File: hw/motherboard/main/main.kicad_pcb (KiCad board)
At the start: 4 copper layers, 100 x 100 mm, 104 parts, among them J1 SWD holes, J2 Conn_ARM_JTAG_SWD_10, J3 690-005-299-043, J4 STACK_GND, Q1 BSS138, SW1 SW_Push, U1 STM32F303RETx, U2 FT232RL-REEL, Y1 HSE

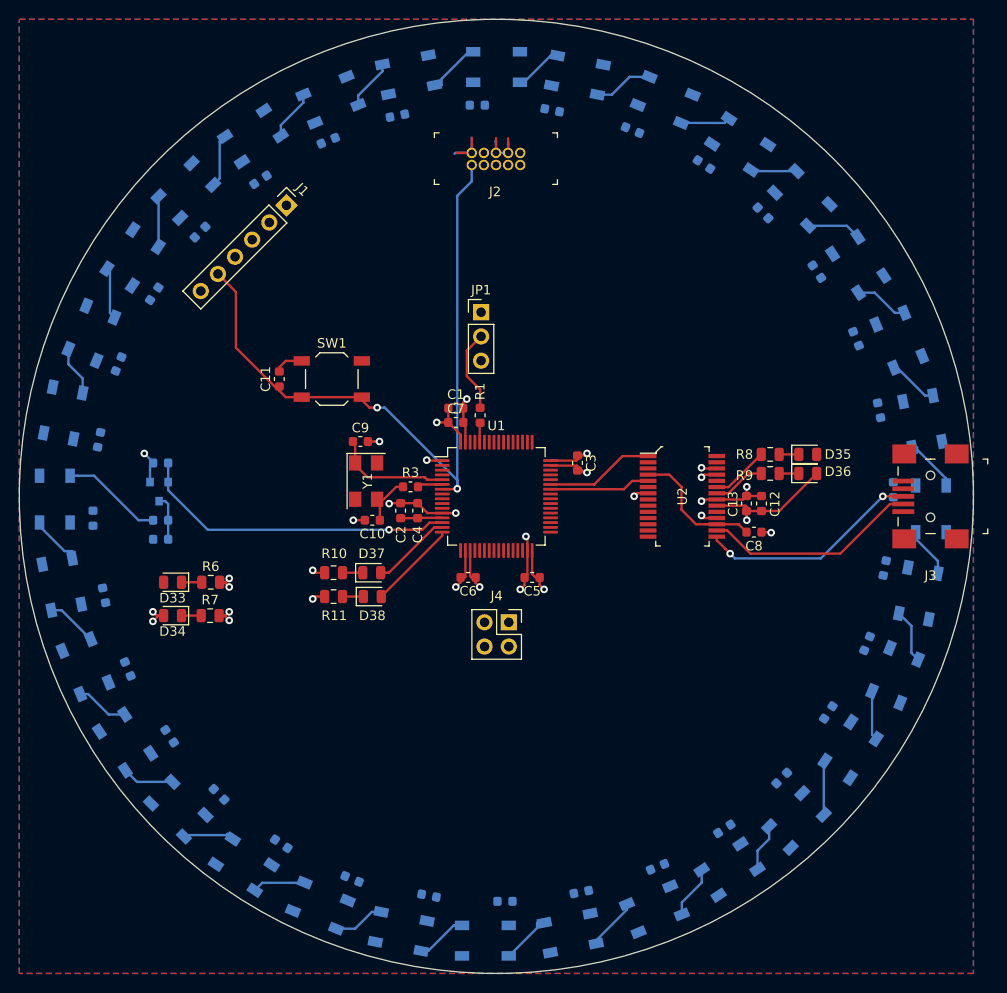
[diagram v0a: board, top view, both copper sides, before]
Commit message: WIP Add electromagnet and sensor schematic connections to MCU pins
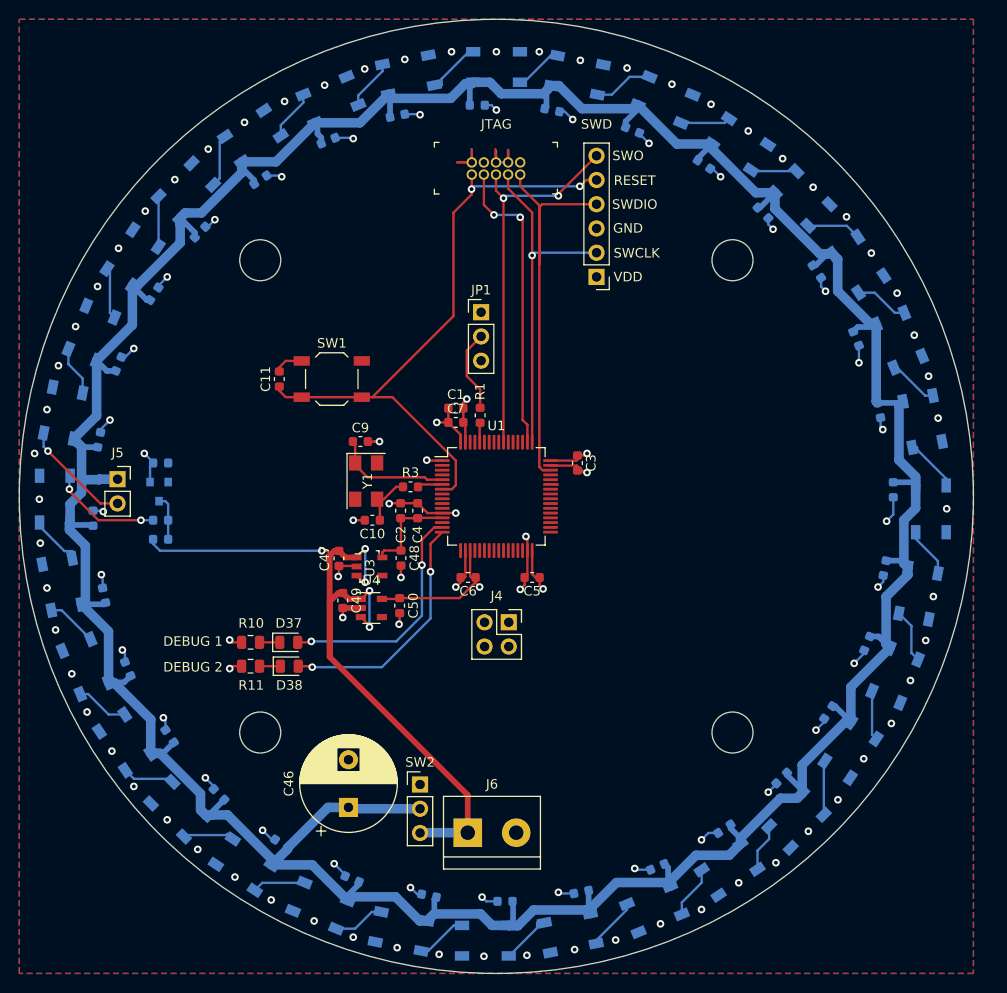
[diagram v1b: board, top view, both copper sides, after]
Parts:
- removed C12: 4.7u, Capacitor_SMD:C_0603_1608Metric
- removed C13, C8: 100n, Capacitor_SMD:C_0603_1608Metric
- removed D33: LED_5V, LED_SMD:LED_0805_2012Metric
- removed D34: LED_3V3, LED_SMD:LED_0805_2012Metric
- removed D35: LED_TX, LED_SMD:LED_0805_2012Metric
- removed D36: LED_RX, LED_SMD:LED_0805_2012Metric
- removed J3: 690-005-299-043, digikey-footprints:USB_Mini_B_Female_690-005-299-043
- removed R6, R7: TBD, Resistor_SMD:R_0805_2012Metric
- removed R8, R9: 1k, Resistor_SMD:R_0805_2012Metric
- removed U2: FT232RL-REEL, digikey-footprints:SSOP-28_W5.30mm
- added C46: 1000u, Capacitor_THT:CP_Radial_D10.0mm_P5.00mm, F.Cu at (134.5, 132.6)
- added C47: 1u, Capacitor_SMD:C_0603_1608Metric, F.Cu at (133.5, 106.5)
- added C48: 1u, Capacitor_SMD:C_0603_1608Metric, F.Cu at (140.0, 106.5)
- added C49: 1u, Capacitor_SMD:C_0603_1608Metric, F.Cu at (133.9, 110.9)
- added C50: 1u, Capacitor_SMD:C_0603_1608Metric, F.Cu at (139.9, 111.5)
- added H1: MountingHole, MountingHole:MountingHole_4.3mm_M4, F.Cu at (174.7, 124.7)
- added H2: MountingHole, MountingHole:MountingHole_4.3mm_M4, F.Cu at (125.3, 124.7)
- added H3: MountingHole, MountingHole:MountingHole_4.3mm_M4, F.Cu at (125.3, 75.3)
- added H4: MountingHole, MountingHole:MountingHole_4.3mm_M4, F.Cu at (174.7, 75.3)
- added J5: RGB stack, Connector_PinSocket_2.54mm:PinSocket_1x02_P2.54mm_Vertical, F.Cu at (110.3, 98.2)
- added J6: 5V power in, TerminalBlock:TerminalBlock_bornier-2_P5.08mm, F.Cu at (147.0, 135.2)
- added SW2: SW_SPDT, Connector_PinHeader_2.54mm:PinHeader_1x03_P2.54mm_Vertical, F.Cu at (142.0, 130.2)
- added U3: LP5907MFX-3_3_NOPB, digikey-footprints:SOT-753, F.Cu at (136.7, 107.3)
- added U4: TLV75533PDBV, Package_TO_SOT_SMD:SOT-23-5, F.Cu at (136.9, 111.7)
- moved J1 33.4 mm to (160.5, 77.0), turned to 180 degrees
- moved R10 11.4 mm to (124.2, 115.3)
- moved R11 11.4 mm to (124.2, 117.8)
- moved D37 11.4 mm to (128.2, 115.3)
- moved D38 11.4 mm to (128.3, 117.8)
- moved J2 1.00 mm to (152.5, 65.0)
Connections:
- net +5V renamed /rgb/5V_RGB
- U1 pad 14: /rgb/DIN -> Net-(U1-Pad14)
- U1 pad 4: Net-(U1-Pad4) -> /rgb/DIN
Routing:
- net /rgb/5V_RGB: track 13.6 -> 405.7 mm, vias 1 -> 0
- net +5V: track 0.00 -> 86.5 mm, vias 0 -> 5
- net /JTAG_TMS: track 0.00 -> 44.9 mm
- net /JTAG_TDO: track 0.00 -> 40.1 mm, vias 0 -> 2
- net GND: track 74.6 -> 112.7 mm, vias 22 -> 109
- net /JTAG_TCK: track 0.00 -> 36.0 mm, vias 0 -> 1
- net /rgb/DIN: track 33.6 -> 0.00 mm, vias 1 -> 0
- net /JTAG_TDI: track 0.00 -> 31.4 mm, vias 0 -> 2
- net /USB_DP: track 23.4 -> 0.00 mm, vias 2 -> 0
- net /USB_DM: track 22.7 -> 0.00 mm
- net /DEBUG_1: track 8.42 -> 24.8 mm, vias 0 -> 2
- net /DEBUG_2: track 9.40 -> 25.6 mm, vias 0 -> 2
- net Net-(C8-Pad1): track 14.2 -> 0.00 mm
- net Net-(D32-Pad2): track 0.00 -> 11.7 mm, vias 0 -> 1
- net /USART1_RX: track 11.5 -> 0.77 mm
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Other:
- net class power added: clearance 1, trace_width 0.25, via_dia 0.8, via_drill 0.4
- board text added: "DEBUG 1"
- board text added: "DEBUG 2"
- board text added: "GND"
- board text added: "JTAG"
- board text added: "RESET"
- board text added: "SWCLK"
- board text added: "SWD"
- board text added: "SWDIO"
- board text added: "SWO"
- board text added: "VDD"

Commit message: Lay out motherboard hardware revision 1
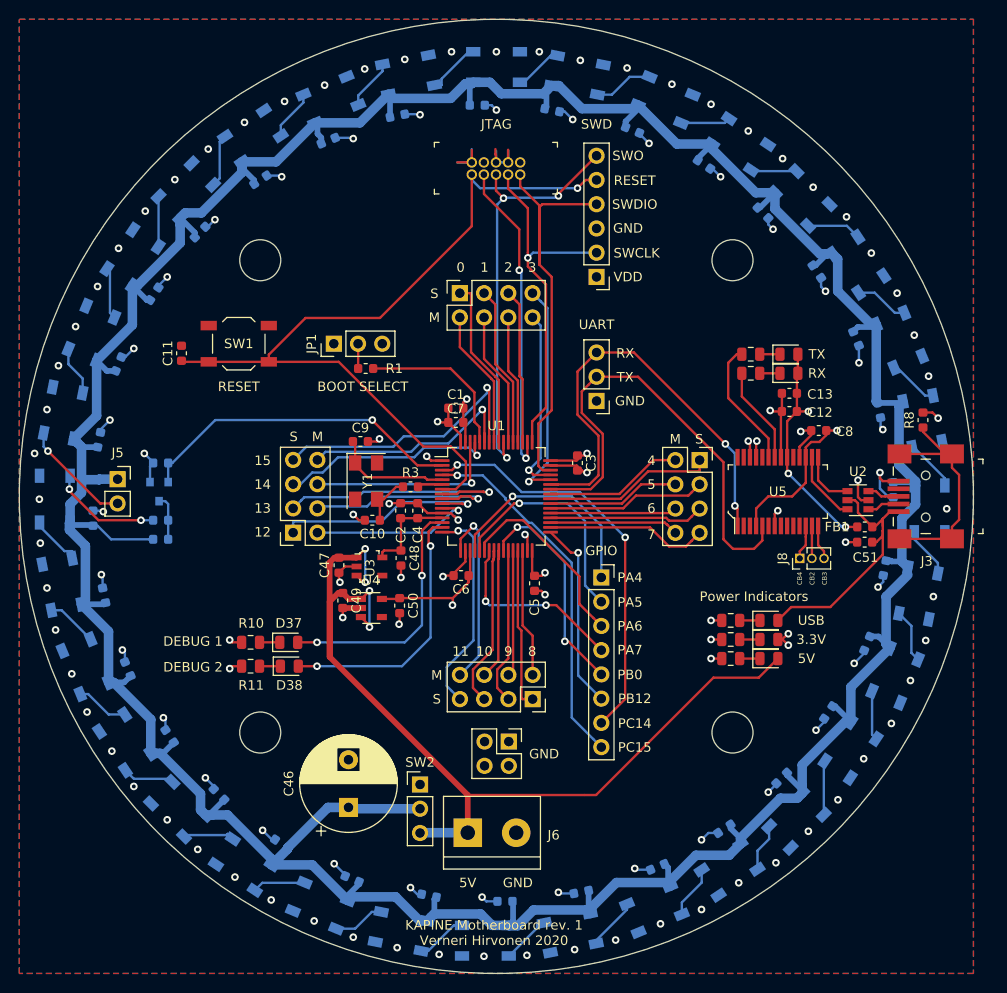
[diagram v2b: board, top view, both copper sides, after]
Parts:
- added C12: 4.7u, Capacitor_SMD:C_0603_1608Metric, F.Cu at (180.7, 91.1)
- added C13: 100n, Capacitor_SMD:C_0603_1608Metric, F.Cu at (180.7, 89.2)
- added C51: 10n, Capacitor_SMD:C_0603_1608Metric, F.Cu at (188.6, 104.8)
- added C8: 100n, Capacitor_SMD:C_0603_1608Metric, F.Cu at (183.8, 93.1)
- added D33: LED_5V, LED_SMD:LED_0805_2012Metric, F.Cu at (178.6, 117.0)
- added D34: LED_3V3, LED_SMD:LED_0805_2012Metric, F.Cu at (178.6, 115.0)
- added D35: LED_TX, LED_SMD:LED_0805_2012Metric, F.Cu at (180.7, 85.1)
- added D36: LED_RX, LED_SMD:LED_0805_2012Metric, F.Cu at (180.7, 87.1)
- added D39: LED_USB, LED_SMD:LED_0805_2012Metric, F.Cu at (178.6, 113.0)
- added FB1: Ferrite_Bead, Inductor_SMD:L_0603_1608Metric, F.Cu at (188.6, 103.2)
- added J10: stack[0..3], Connector_PinSocket_2.54mm:PinSocket_2x04_P2.54mm_Vertical, F.Cu at (171.3, 96.2)
- added J11: stack[0..3], Connector_PinSocket_2.54mm:PinSocket_2x04_P2.54mm_Vertical, F.Cu at (153.8, 121.2)
- added J12: stack[0..3], Connector_PinSocket_2.54mm:PinSocket_2x04_P2.54mm_Vertical, F.Cu at (128.7, 103.8)
- added J13: GPIO, Connector_PinSocket_2.54mm:PinSocket_1x08_P2.54mm_Vertical, F.Cu at (161.0, 108.5)
- added J3: 690-005-299-043, digikey-footprints:USB_Mini_B_Female_690-005-299-043, F.Cu at (195.0, 100.0)
- added J7: UART pins, Connector_PinHeader_2.54mm:PinHeader_1x03_P2.54mm_Vertical, F.Cu at (160.5, 90.0)
- added J8: CBUS[2..4], Connector_PinHeader_1.27mm:PinHeader_1x03_P1.27mm_Vertical, F.Cu at (181.8, 106.5)
- added J9: stack[0..3], Connector_PinSocket_2.54mm:PinSocket_2x04_P2.54mm_Vertical, F.Cu at (146.2, 78.7)
- added R12: 1k, Resistor_SMD:R_0805_2012Metric, F.Cu at (176.7, 87.1)
- added R13: 1k, Resistor_SMD:R_0805_2012Metric, F.Cu at (174.6, 113.0)
- added R6: TBD, Resistor_SMD:R_0805_2012Metric, F.Cu at (174.6, 117.0)
- added R7: TBD, Resistor_SMD:R_0805_2012Metric, F.Cu at (174.6, 115.0)
- added R8: 0, Resistor_SMD:R_0603_1608Metric, F.Cu at (194.7, 92.0)
- added R9: 1k, Resistor_SMD:R_0805_2012Metric, F.Cu at (176.7, 85.1)
- added U2: USBLC6-2SC6, Package_TO_SOT_SMD:SOT-23-6, F.Cu at (187.9, 100.4)
- added U5: FT232RL-REEL, digikey-footprints:SSOP-28_W5.30mm, F.Cu at (179.5, 99.5)
- moved JP1 15.8 mm to (133.0, 84.0), turned to 90 degrees
- moved R1 13.0 mm to (136.3, 86.6), turned to 180 degrees
- moved J4 12.5 mm to (151.3, 125.7)
- moved C11 10.6 mm to (117.0, 85.0)
- moved SW1 10.4 mm to (123.0, 84.0)
- moved C6 0.76 mm to (146.3, 108.3)
- moved C47 0.71 mm to (133.5, 107.2)
- moved C5 0.66 mm to (154.0, 109.1), turned to 270 degrees
- moved D17 0.14 mm to (195.4, 101.3)
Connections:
- U1 pad 10: Net-(U1-Pad10) -> /s12
- U1 pad 11: Net-(U1-Pad11) -> /m12
- U1 pad 14: Net-(U1-Pad14) -> /DEBUG_1
- U1 pad 15: /DEBUG_1 -> /DEBUG_2
- U1 pad 16: /DEBUG_2 -> /s11
- U1 pad 17: Net-(U1-Pad17) -> /m11
- U1 pad 2: Net-(U1-Pad2) -> /rgb/DIN
- U1 pad 20: Net-(U1-Pad20) -> /PA4
- U1 pad 21: Net-(U1-Pad21) -> /PA5
- U1 pad 22: Net-(U1-Pad22) -> /PA6
- U1 pad 23: Net-(U1-Pad23) -> /PA7
- U1 pad 24: Net-(U1-Pad24) -> /s10
- U1 pad 25: Net-(U1-Pad25) -> /m10
- U1 pad 26: Net-(U1-Pad26) -> /PB0
- U1 pad 27: Net-(U1-Pad27) -> /s9
- U1 pad 28: Net-(U1-Pad28) -> /m9
- U1 pad 29: Net-(U1-Pad29) -> /s8
- U1 pad 3: Net-(U1-Pad3) -> /PC14
- U1 pad 30: Net-(U1-Pad30) -> /m8
- U1 pad 33: Net-(U1-Pad33) -> /PB12
- U1 pad 34: Net-(U1-Pad34) -> /s7
- U1 pad 35: Net-(U1-Pad35) -> /m7
- U1 pad 36: Net-(U1-Pad36) -> /s6
- U1 pad 37: Net-(U1-Pad37) -> /m6
- U1 pad 38: Net-(U1-Pad38) -> /s5
- U1 pad 39: Net-(U1-Pad39) -> /m5
- U1 pad 4: /rgb/DIN -> /PC15
- U1 pad 40: Net-(U1-Pad40) -> /s4
- U1 pad 41: Net-(U1-Pad41) -> /m4
- U1 pad 44: Net-(U1-Pad44) -> /s3
- U1 pad 45: Net-(U1-Pad45) -> /m3
- U1 pad 51: Net-(U1-Pad51) -> /s2
- U1 pad 52: Net-(U1-Pad52) -> /m2
- U1 pad 53: Net-(U1-Pad53) -> /s1
- U1 pad 54: Net-(U1-Pad54) -> /m1
- U1 pad 56: Net-(U1-Pad56) -> /s0
- U1 pad 57: Net-(U1-Pad57) -> /m0
- U1 pad 58: Net-(U1-Pad58) -> /s15
- U1 pad 59: Net-(U1-Pad59) -> /m15
- U1 pad 61: Net-(U1-Pad61) -> /s14
- U1 pad 62: Net-(U1-Pad62) -> /m14
- U1 pad 8: Net-(U1-Pad8) -> /s13
- U1 pad 9: Net-(U1-Pad9) -> /m13
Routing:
- net /USART1_TX: track 0.04 -> 49.6 mm
- net /USART1_RX: track 0.77 -> 46.6 mm, vias 0 -> 2
- net /PC14: track 0.00 -> 43.0 mm, vias 0 -> 2
- net /PC15: track 0.00 -> 38.1 mm, vias 0 -> 1
- net /rgb/DIN: track 0.00 -> 34.6 mm, vias 0 -> 1
- net /s15: track 0.00 -> 29.6 mm, vias 0 -> 1
- net VBUS: track 0.00 -> 28.0 mm
- net /s13: track 0.00 -> 26.3 mm, vias 0 -> 1
- net GND: track 112.7 -> 138.1 mm, vias 109 -> 119
- net Net-(J3-PadSH): track 0.00 -> 25.0 mm
- net /m15: track 0.00 -> 23.9 mm, vias 0 -> 1
- net /PA5: track 0.00 -> 23.8 mm, vias 0 -> 1
- net VCC: track 0.00 -> 23.8 mm, vias 0 -> 3
- net /s3: track 0.00 -> 23.6 mm, vias 0 -> 1
- net /PA4: track 0.00 -> 23.3 mm, vias 0 -> 1
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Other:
- net class power removed
- board text added: "0"
- board text added: "1"
- board text added: "10"
- board text added: "11"
- board text added: "12"
- board text added: "13"
- board text added: "14"
- board text added: "15"
- board text added: "2"
- board text added: "3"
- board text added: "3.3V"
- board text added: "4"
- board text added: "5"
- board text added: "5V"
- board text added: "6"
- board text added: "7"
- board text added: "8"
- board text added: "9"
- board text added: "BOOT SELECT"
- board text added: "CB2"
- board text added: "CB3"
- board text added: "CB4"
- board text added: "GPIO"
- board text added: "KAPINE Motherboard rev. 1 Verneri Hirvonen 2020"
- board text added: "M"
- board text added: "PA4"
- board text added: "PA5"
- board text added: "PA6"
- board text added: "PA7"
- board text added: "PB0"
- board text added: "PB12"
- board text added: "PC14"
- board text added: "PC15"
- board text added: "Power Indicators"
- board text added: "RX"
- board text added: "S"
- board text added: "TX"
- board text added: "UART"
- board text added: "USB"

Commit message: Minor motherboard layout changes. Bump revision number to 1.1.
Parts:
- removed SW2: SW_SPDT, Connector_PinHeader_2.54mm:PinHeader_1x03_P2.54mm_Vertical
- added JP2: RGB ENABLE, Connector_PinHeader_2.54mm:PinHeader_1x02_P2.54mm_Vertical, F.Cu at (138.5, 122.3)
- C46: footprint Capacitor_THT:CP_Radial_D10.0mm_P5.00mm -> Capacitor_SMD:CP_Elec_10x10
- moved R1 9.55 mm to (145.8, 88.0)
- moved C46 1.84 mm to (135.9, 131.4), turned to 180 degrees
- moved JP1 1.25 mm to (133.0, 85.2)
- moved J4 0.63 mm to (151.2, 126.3)
- moved C6 0.62 mm to (146.9, 108.2)
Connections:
- R4 pad 1: /rgb/5V_RGB -> +5V
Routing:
- net Net-(R1-Pad1): track 17.1 -> 7.29 mm
- net Net-(JP1-Pad2): track 2.62 -> 10.6 mm
- net GND: track 138.1 -> 144.2 mm, vias 119 -> 128
- net /s11: track 22.3 -> 18.3 mm
- net +5V: track 104.3 -> 107.1 mm, vias 4 -> 1
- net /rgb/5V_RGB: track 411.1 -> 413.6 mm, vias 0 -> 3
- net VDD: track 38.9 -> 40.7 mm, vias 8 -> 9
- net /m11: track 19.8 -> 18.1 mm
- net /s13: track 26.3 -> 25.6 mm
- net /RESET#: vias 2 -> 1
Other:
- board text added: "FLASH"
- board text added: "KAPINE Motherboard rev. 1.1 Verneri Hirvonen 2020"
- board text added: "RGB"
- board text added: "RGB ON"
- board text added: "VDD/3.3V"
- board text removed: "3.3V"
- board text removed: "KAPINE Motherboard rev. 1 Verneri Hirvonen 2020"

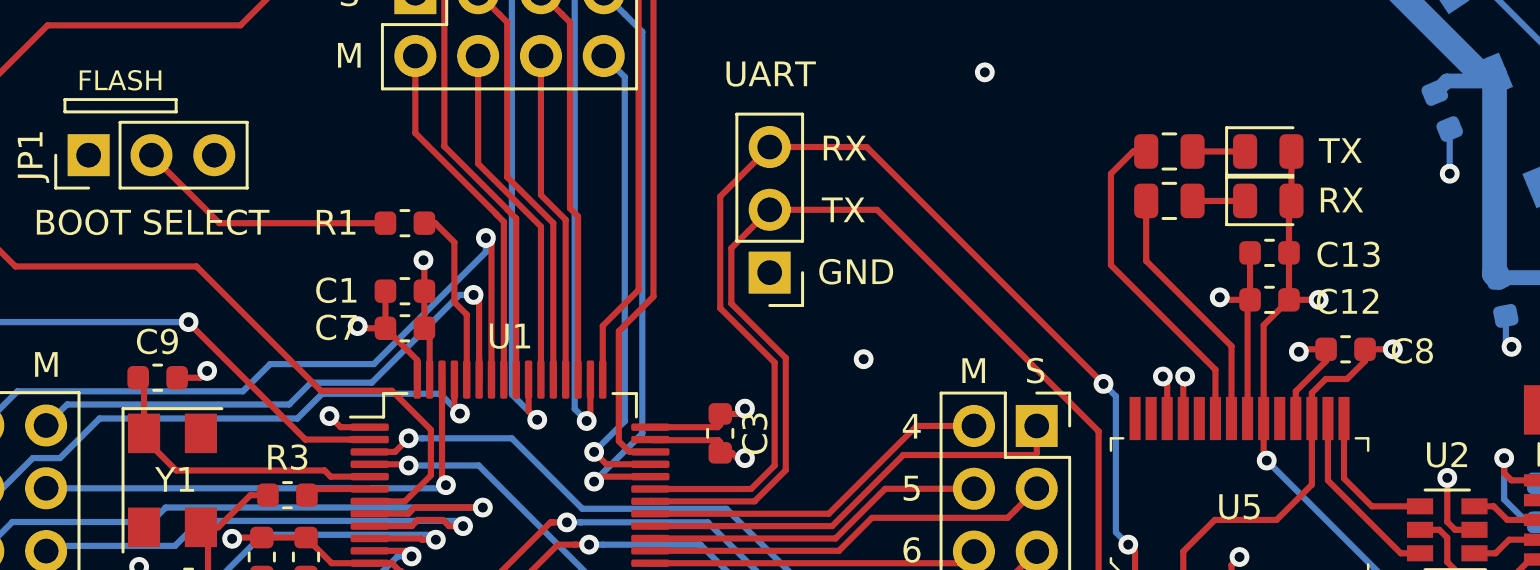
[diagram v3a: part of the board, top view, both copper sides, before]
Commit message: Add missing component values.
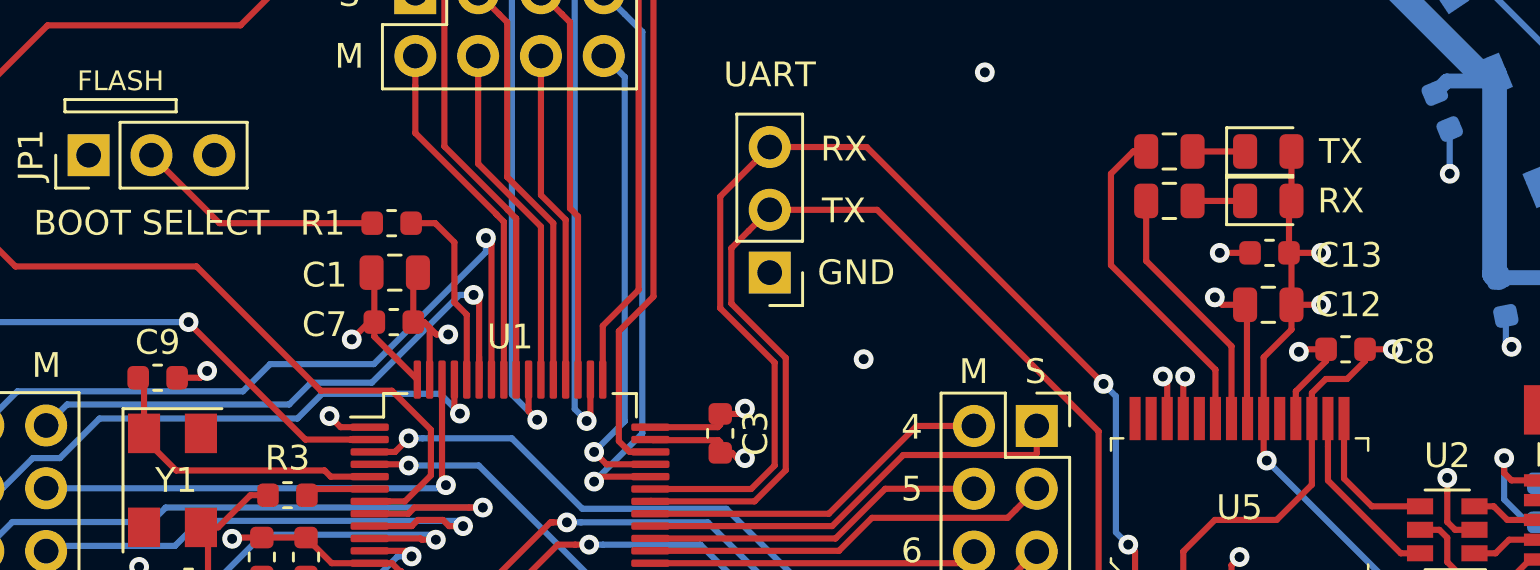
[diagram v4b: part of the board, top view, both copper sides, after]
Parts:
- C1, C12: footprint Capacitor_SMD:C_0603_1608Metric -> Capacitor_SMD:C_0805_2012Metric
- moved C1 0.86 mm to (145.3, 90.0)
- moved R1 0.54 mm to (145.2, 88.0)
- moved C7 0.51 mm to (145.3, 92.0)
- moved C12 0.21 mm to (180.7, 91.3)
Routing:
- net VCC: track 23.8 -> 25.1 mm, vias 3 -> 4
- net VDD: track 40.7 -> 41.7 mm
- net Net-(R1-Pad1): track 7.29 -> 7.83 mm
- net Net-(JP1-Pad2): track 10.6 -> 10.1 mm
- net GND: track 144.2 -> 144.6 mm, vias 128 -> 129
